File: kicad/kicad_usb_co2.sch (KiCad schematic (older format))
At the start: 6 parts, among them SW1 SW_SPDT, SW2 SW_SPDT, U1 MH-Z19B, U2 SeeeduinoXIAO

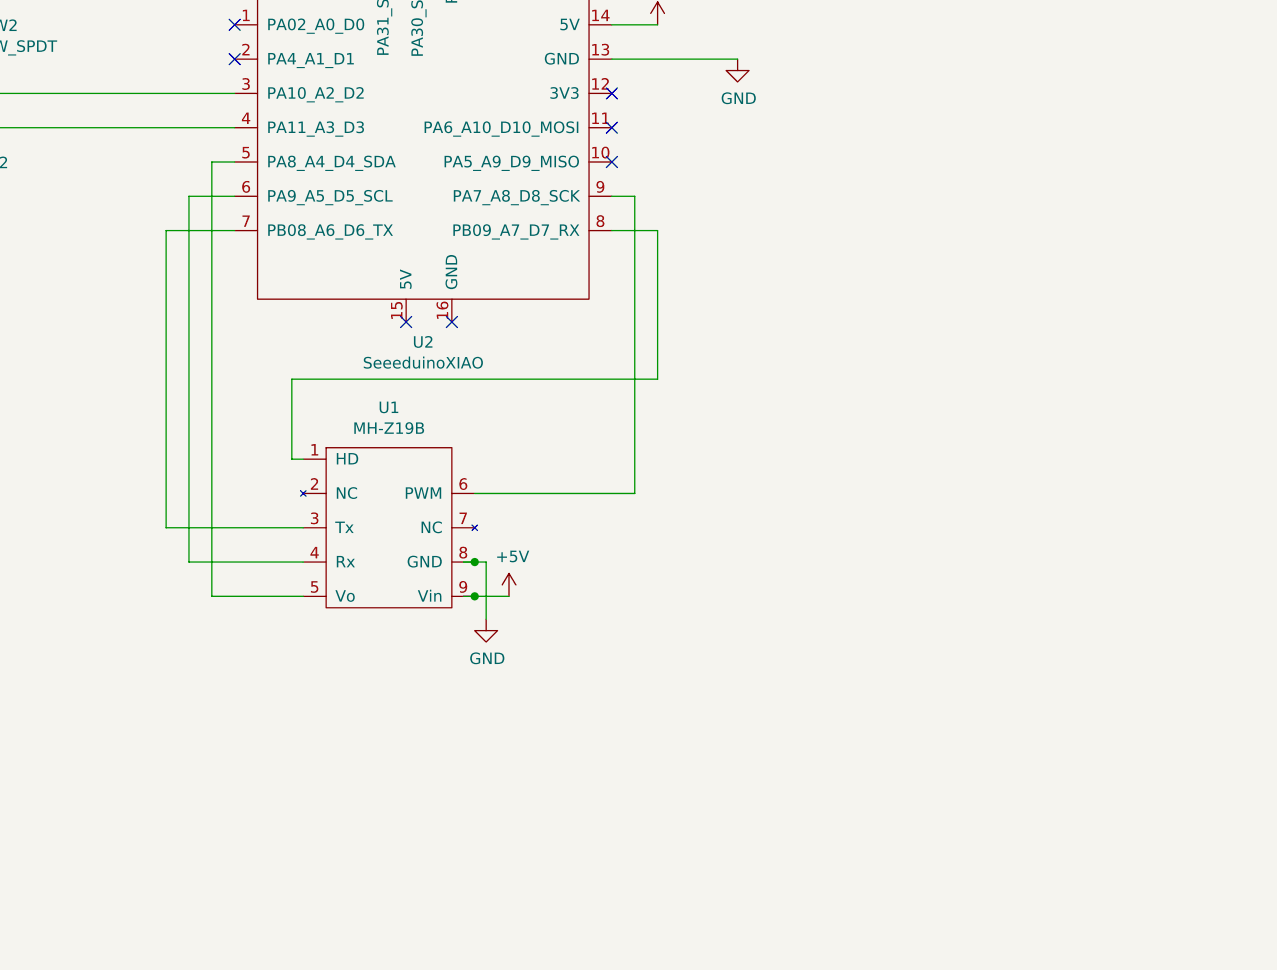
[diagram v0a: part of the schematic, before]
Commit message: スキーマにMH-Z14AとMH-Z19Bを共存させた
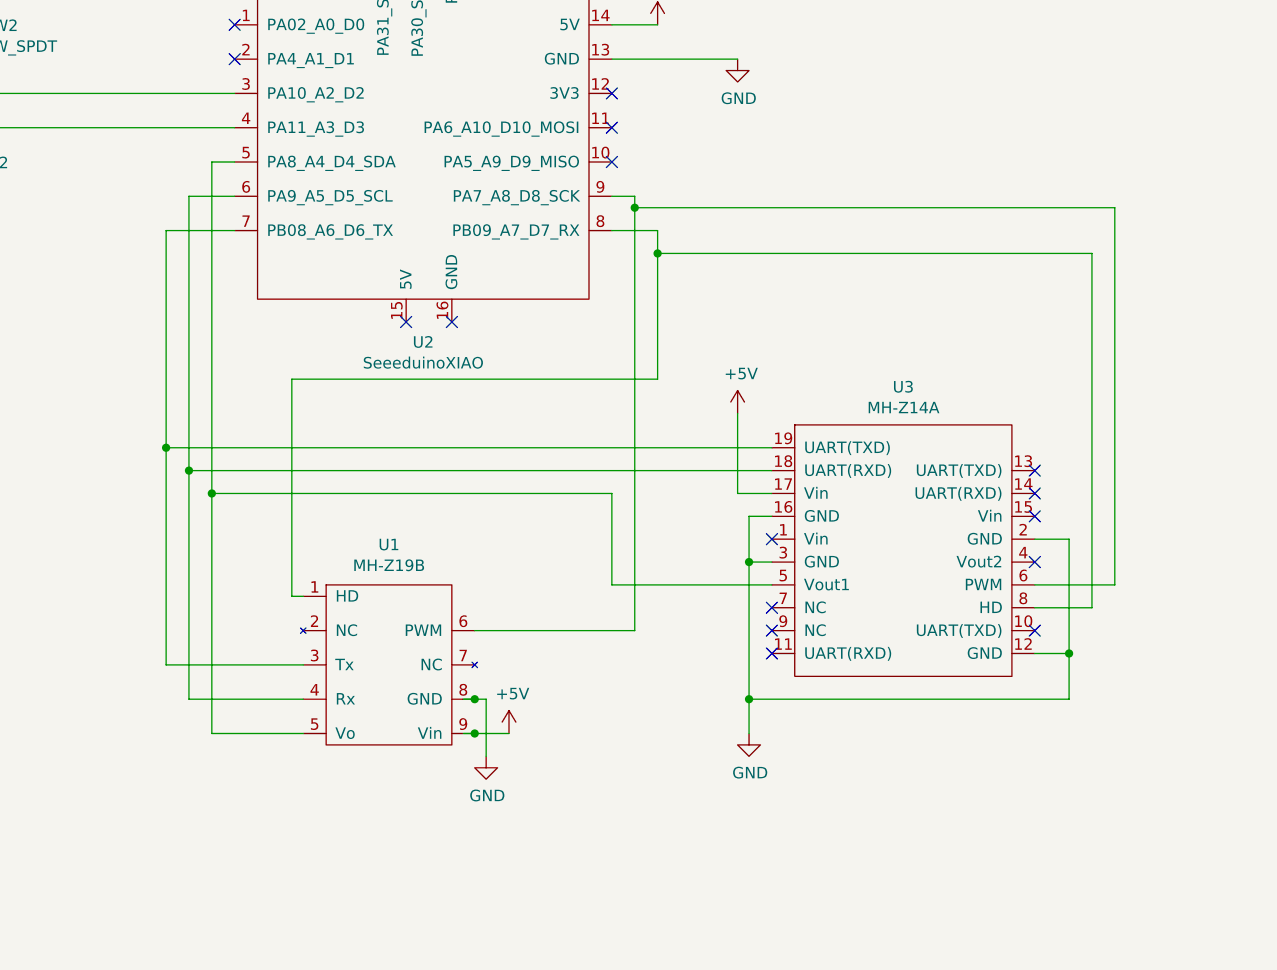
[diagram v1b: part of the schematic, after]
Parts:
- removed U1: MH-Z19B, MH-Z19B:MH-Z19B, symbol MH-Z19B:MH-Z19B
- added U1: MH-Z19B, kicad_mylib:MH-Z19B, symbol kicad_mylib:MH-Z19B
- added U3: MH-Z14A, My_lib:MH-Z14A, symbol kicad_mylib:MH-Z14A
- U2: footprint Seeeduino XIAO:Seeeduino XIAO-MOUDLE14P-2.54-21X17.8MM -> kicad_mylib:SeeedXIAO
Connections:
- wire segments 34 -> 62
- no-connect marks 13 -> 22
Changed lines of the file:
@@
 	1    0    0    -1
 $EndComp
-Wire Wire Line
-	1750 2650 1750 2700
-Wire Wire Line
-	2900 2700 1750 2700
-Connection ~ 1750 2700
-Wire Wire Line
-	1750 2700 1750 2900
-Wire Wire Line
-	2900 2850 1200 2850
-Wire Wire Line
-	1200 2800 1200 2850
-Connection ~ 1200 2850
-Wire Wire Line
-	1200 2850 1200 3050
 NoConn ~ 4550 2700
 NoConn ~ 4550 3000
@@
 NoConn ~ 3700 1950
 NoConn ~ 3550 1950
-NoConn ~ 3850 3700
-NoConn ~ 3650 3700
 $Comp
 L power:PWR_FLAG #FLG0101
@@
 L power:GND #PWR0107
 U 1 1 5EF09D7E
-P 4000 5000
-F 0 "#PWR0107" H 4000 4750 50  0001 C CNN
-F 1 "GND" H 4005 4827 50  0000 C CNN
-F 2 "" H 4000 5000 50  0001 C CNN
-F 3 "" H 4000 5000 50  0001 C CNN
-	1    4000 5000
+P 4000 5600
+F 0 "#PWR0107" H 4000 5350 50  0001 C CNN
+F 1 "GND" H 4005 5427 50  0000 C CNN
+F 2 "" H 4000 5600 50  0001 C CNN
+F 3 "" H 4000 5600 50  0001 C CNN
+	1    4000 5600
 	1    0    0    -1
 $EndComp
@@
 Wire Wire Line
 	4750 2400 4550 2400
-$Comp
-L Seeeduino_XIAO:SeeeduinoXIAO U2
-U 1 1 5F3D41B4
-P 3750 2850
-F 0 "U2" H 3725 1911 50  0000 C CNN
-F 1 "SeeeduinoXIAO" H 3725 1820 50  0000 C CNN
-F 2 "Seeeduino XIAO:Seeeduino XIAO-MOUDLE14P-2.54-21X17.8MM" H 3400 3050 50  0001 C CNN
-F 3 "" H 3400 3050 50  0001 C CNN
-	1    3750 2850
-	1    0    0    -1
-$EndComp
 $Comp
 L Switch:SW_SPDT SW2
@@
 NoConn ~ 1000 2800
 Wire Wire Line
-	4000 4750 4000 5000
-Wire Wire Line
-	4100 4900 3950 4900
-Wire Wire Line
-	3900 4750 3950 4750
-$Comp
-L MH-Z19B:MH-Z19B U1
-U 1 1 5F7ADA5F
-P 3200 4300
-F 0 "U1" H 3575 4525 50  0000 C CNN
-F 1 "MH-Z19B" H 3575 4434 50  0000 C CNN
-F 2 "MH-Z19B:MH-Z19B" H 3300 4400 50  0001 C CNN
-F 3 "" H 3300 4400 50  0001 C CNN
-	1    3200 4300
-	1    0    0    -1
-$EndComp
-Connection ~ 3950 4750
-Wire Wire Line
-	3950 4750 4000 4750
-Connection ~ 3950 4900
-Wire Wire Line
-	3950 4900 3900 4900
-Wire Wire Line
-	4750 3950 3150 3950
-Wire Wire Line
-	3150 3950 3150 4300
-Wire Wire Line
-	3150 4300 3200 4300
-Wire Wire Line
-	4650 4450 3950 4450
-Wire Wire Line
-	2800 4900 3200 4900
-Wire Wire Line
-	2600 4600 3200 4600
-Wire Wire Line
-	2700 4750 3200 4750
+	4000 5350 4000 5600
+Wire Wire Line
+	3150 4900 3200 4900
+Wire Wire Line
+	2800 5500 3200 5500
+Wire Wire Line
+	2600 5200 3200 5200
+Wire Wire Line
+	2700 5350 3200 5350
 Wire Wire Line
 	2900 3000 2800 3000
 Wire Wire Line
-	2800 3000 2800 4900
-Wire Wire Line
 	2900 3150 2700 3150
 Wire Wire Line
-	2700 3150 2700 4750
-Wire Wire Line
 	2900 3300 2600 3300
 Wire Wire Line
-	2600 3300 2600 4600
-Wire Wire Line
 	4550 3150 4650 3150
 Wire Wire Line
-	4650 3150 4650 4450
-Wire Wire Line
 	4550 3300 4750 3300
-Wire Wire Line
-	4750 3300 4750 3950
 $Comp
 L power:+5V #PWR01
@@
 L power:+5V #PWR05
 U 1 1 5F8A88E4
-P 4100 4900
-F 0 "#PWR05" H 4100 4750 50  0001 C CNN
-F 1 "+5V" H 4115 5073 50  0000 C CNN
-F 2 "" H 4100 4900 50  0001 C CNN
-F 3 "" H 4100 4900 50  0001 C CNN
-	1    4100 4900
-	1    0    0    -1
-$EndComp
+P 4100 5500
+F 0 "#PWR05" H 4100 5350 50  0001 C CNN
+F 1 "+5V" H 4115 5673 50  0000 C CNN
+F 2 "" H 4100 5500 50  0001 C CNN
+F 3 "" H 4100 5500 50  0001 C CNN
+	1    4100 5500
+	1    0    0    -1
+$EndComp
+Wire Wire Line
+	3900 5500 3950 5500
+Wire Wire Line
+	3900 5350 3950 5350
+Wire Wire Line
+	4750 3300 4750 3400
+Wire Wire Line
+	4650 5050 3950 5050
+Wire Wire Line
+	4750 3950 3150 3950
+$Comp
+L Seeeduino_XIAO:SeeeduinoXIAO U2
+U 1 1 5F3D41B4
+P 3750 2850
+F 0 "U2" H 3725 1911 50  0000 C CNN
+F 1 "SeeeduinoXIAO" H 3725 1820 50  0000 C CNN
+F 2 "kicad_mylib:SeeedXIAO" H 3400 3050 50  0001 C CNN
+F 3 "" H 3400 3050 50  0001 C CNN
+	1    3750 2850
+	1    0    0    -1
+$EndComp
+NoConn ~ 3650 3700
+NoConn ~ 3850 3700
+$Comp
+L kicad_mylib:MH-Z19B U1
+U 1 1 5F99039B
+P 3200 4900
+F 0 "U1" H 3575 5125 50  0000 C CNN
+F 1 "MH-Z19B" H 3575 5034 50  0000 C CNN
+F 2 "kicad_mylib:MH-Z19B" H 3300 5000 50  0001 C CNN
+F 3 "" H 3300 5000 50  0001 C CNN
+	1    3200 4900
+	1    0    0    -1
+$EndComp
+Connection ~ 3950 5350
+Wire Wire Line
+	3950 5350 4000 5350
+Connection ~ 3950 5500
+Wire Wire Line
+	3950 5500 4100 5500
+$Comp
+L kicad_mylib:MH-Z14A U3
+U 1 1 5F991482
+P 5250 4250
+F 0 "U3" H 5825 4515 50  0000 C CNN
+F 1 "MH-Z14A" H 5825 4424 50  0000 C CNN
+F 2 "My_lib:MH-Z14A" H 5400 4400 50  0001 C CNN
+F 3 "" H 5400 4400 50  0001 C CNN
+	1    5250 4250
+	1    0    0    -1
+$EndComp
+Wire Wire Line
+	2600 3300 2600 4250
+Wire Wire Line
+	2700 3150 2700 4350
+Wire Wire Line
+	2800 3000 2800 4450
+Wire Wire Line
+	3150 3950 3150 4900
+Wire Wire Line
+	4650 3150 4650 3200
+Wire Wire Line
+	5250 4250 2600 4250
+Connection ~ 2600 4250
+Wire Wire Line
+	2600 4250 2600 5200
+Wire Wire Line
+	5250 4350 2700 4350
+Connection ~ 2700 4350
+Wire Wire Line
+	2700 4350 2700 5350
+$Comp
+L power:+5V #PWR06
+U 1 1 5F996856
+P 5100 4100
+F 0 "#PWR06" H 5100 3950 50  0001 C CNN
+F 1 "+5V" H 5115 4273 50  0000 C CNN
+F 2 "" H 5100 4100 50  0001 C CNN
+F 3 "" H 5100 4100 50  0001 C CNN
+	1    5100 4100
+	1    0    0    -1
+$EndComp
+$Comp
+L power:GND #PWR07
+U 1 1 5F996FA2
+P 5150 5500
+F 0 "#PWR07" H 5150 5250 50  0001 C CNN
+F 1 "GND" H 5155 5327 50  0000 C CNN
+F 2 "" H 5150 5500 50  0001 C CNN
+F 3 "" H 5150 5500 50  0001 C CNN
+	1    5150 5500
+	1    0    0    -1
+$EndComp
+Wire Wire Line
+	5100 4100 5100 4450
+Wire Wire Line
+	5100 4450 5250 4450
+Wire Wire Line
+	5250 4550 5150 4550
+Wire Wire Line
+	5150 4550 5150 4750
+Wire Wire Line
+	5250 4750 5150 4750
+Connection ~ 5150 4750
+Wire Wire Line
+	5150 4750 5150 5350
+Wire Wire Line
+	5150 5350 6550 5350
+Wire Wire Line
+	6550 5350 6550 5150
+Wire Wire Line
+	6550 4650 6400 4650
+Connection ~ 5150 5350
+Wire Wire Line
+	5150 5350 5150 5500
+Wire Wire Line
+	6400 5150 6550 5150
+Connection ~ 6550 5150
+Wire Wire Line
+	6550 5150 6550 4650
+NoConn ~ 5250 4650
+Wire Wire Line
+	5250 4850 4550 4850
+Wire Wire Line
+	4550 4850 4550 4450
+Wire Wire Line
+	4550 4450 2800 4450
+Connection ~ 2800 4450
+Wire Wire Line
+	2800 4450 2800 5500
+Wire Wire Line
+	6400 4950 6650 4950
+Wire Wire Line
+	6650 4950 6650 3400
+Wire Wire Line
+	6650 3400 4750 3400
+Connection ~ 4750 3400
+Wire Wire Line
+	4750 3400 4750 3950
+Wire Wire Line
+	6400 4850 6750 4850
+Wire Wire Line
+	6750 4850 6750 3200
+Wire Wire Line
+	6750 3200 4650 3200
+Connection ~ 4650 3200
+Wire Wire Line
+	4650 3200 4650 5050
+NoConn ~ 6400 4350
+NoConn ~ 6400 4450
+NoConn ~ 6400 4550
+NoConn ~ 6400 4750
+NoConn ~ 6400 5050
+NoConn ~ 5250 5050
+NoConn ~ 5250 4950
+NoConn ~ 5250 5150
+Connection ~ 1200 2850
+Wire Wire Line
+	1200 2850 1200 3050
+Wire Wire Line
+	1200 2800 1200 2850
+Connection ~ 1750 2700
+Wire Wire Line
+	1750 2700 1750 2900
+Wire Wire Line
+	1750 2650 1750 2700
+Wire Wire Line
+	2900 2850 1200 2850
+Wire Wire Line
+	2900 2700 1750 2700
 $EndSCHEMATC
